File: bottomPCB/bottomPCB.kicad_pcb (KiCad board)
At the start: 2 copper layers, 184.8 x 139 mm, 47 parts, among them J1 Conn_01x03_Pin, J2 Conn_02x03_Odd_Even, J3 Conn_01x02, J4 Conn_02x03_Odd_Even, U1 ESP32-WROOM-32, U2 XT30_horizontal, U3 XT30_horizontal, U8 LM1117IMPX-3_3_NOPB, U9 LM1117IMPX-3_3_NOPB

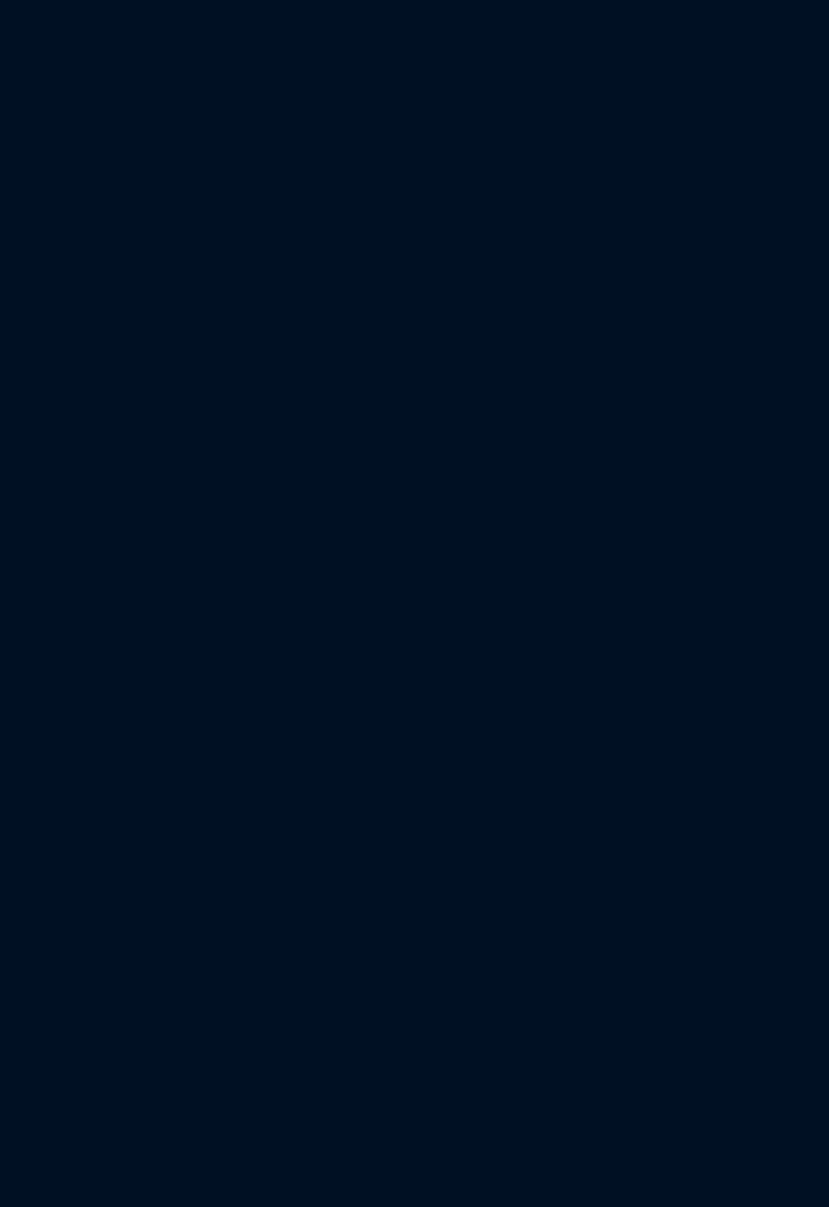
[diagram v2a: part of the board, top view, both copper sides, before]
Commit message: added vertical escon driver
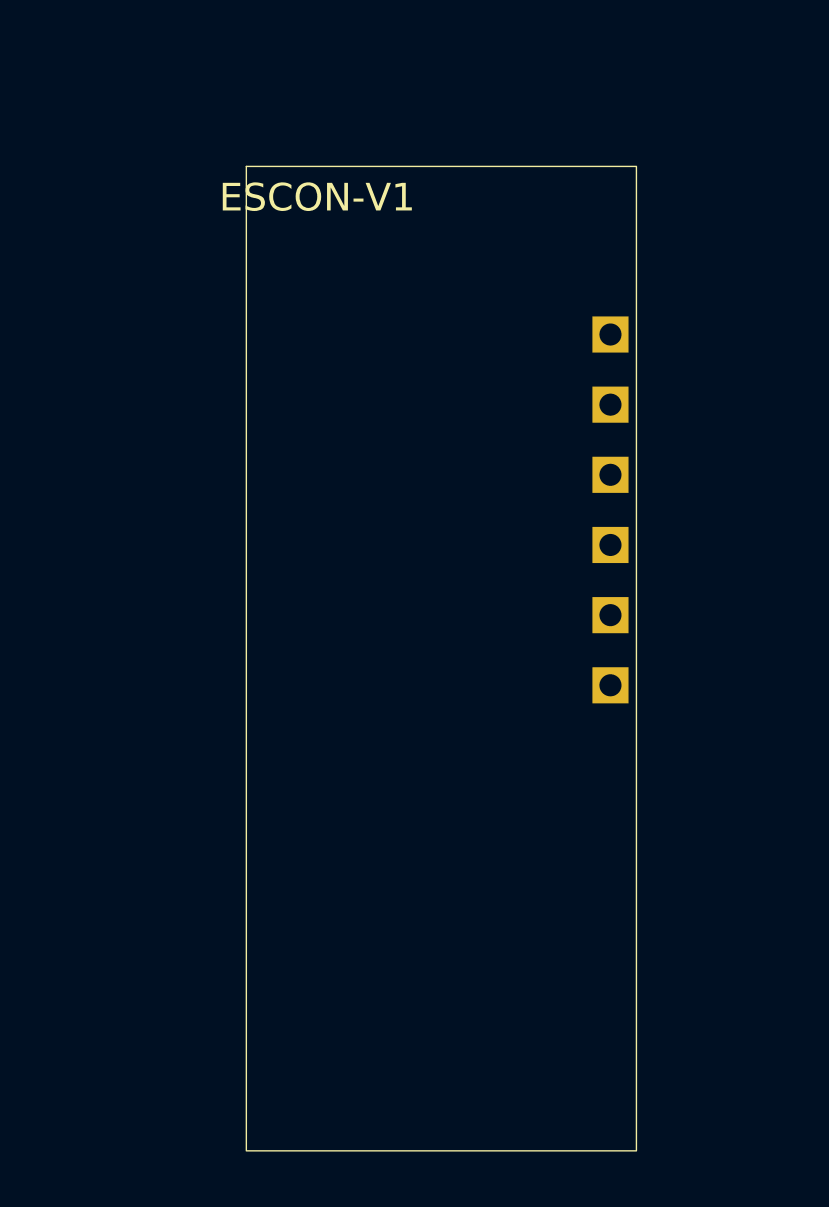
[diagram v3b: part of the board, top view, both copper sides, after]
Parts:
- added ESCON-V1: ~, sarcat:ESCON-V, F.Cu at (118.4, 98.0)
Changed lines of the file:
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@@
 	(net 86 "unconnected-(U3-Pad3)")
 	(net 87 "unconnected-(U3-Pad4)")
+	(net 88 "unconnected-(ESCON-V1-GND-Pad5)")
+	(net 89 "unconnected-(ESCON-V1-VCC-Pad6)")
+	(net 90 "unconnected-(ESCON-V1-D1-Pad1)")
+	(net 91 "unconnected-(ESCON-V1-D3-Pad3)")
+	(net 92 "unconnected-(ESCON-V1-D4-Pad4)")
+	(net 93 "unconnected-(ESCON-V1-D2-Pad2)")
 	(footprint "BohleBots:SOT-223_L6.5-W3.5-P2.30-LS7.0-BR"
 		(layer "F.Cu")
@@
 		(fp_arc
 			(start 1.390018 0.400203)
-			(mid 1.299267 0.619284)
+			(mid 1.299267 0.61928)
 			(end 1.080188 0.710033)
 			(stroke
@@
 		(tags "connector JST PH side entry")
 		(property "Reference" "JP2"
-			(at 7 -2.9 270)
+			(at 7 -2.9 -90)
 			(layer "F.SilkS")
 			(effects
@@
 		)
 		(property "Value" "B8B-PH-K"
-			(at 7 4.000001 270)
+			(at 7 4.000001 -90)
 			(layer "F.Fab")
 			(effects
@@
 				(font
 					(size 1.27 1.27)
+					(thickness 0.15)
 				)
 			)
@@
 				(font
 					(size 1.27 1.27)
+					(thickness 0.15)
 				)
 			)
@@
 				(font
 					(size 1.27 1.27)
+					(thickness 0.15)
 				)
 			)
@@
 		)
 		(fp_text user "${REFERENCE}"
-			(at 7 1.5 270)
+			(at 7 1.5 -90)
 			(layer "F.Fab")
 			(effects
@@
 		)
 	)
+	(footprint "sarcat:ESCON-V"
+		(layer "F.Cu")
+		(at 118.3786 98.0348)
+		(property "Reference" "ESCON-V1"
+			(at -4.4958 -16.6878 0)
+			(unlocked yes)
+			(layer "F.SilkS")
+			(effects
+				(font
+					(size 1 1)
+					(thickness 0.1)
+				)
+			)
+		)
+		(property "Value" "~"
+			(at -2 -9 0)
+			(unlocked yes)
+			(layer "F.Fab")
+			(effects
+				(font
+					(size 1 1)
+					(thickness 0.15)
+				)
+			)
+		)
+		(property "Footprint" "sarcat:ESCON-V"
+			(at -2 -10 0)
+			(unlocked yes)
+			(layer "F.Fab")
+			(hide yes)
+			(effects
+				(font
+					(size 1 1)
+					(thickness 0.15)
+				)
+			)
+		)
+		(property "Datasheet" ""
+			(at -2 -10 0)
+			(unlocked yes)
+			(layer "F.Fab")
+			(hide yes)
+			(effects
+				(font
+					(size 1 1)
+					(thickness 0.15)
+				)
+			)
+		)
+		(property "Description" ""
+			(at -2 -10 0)
+			(unlocked yes)
+			(layer "F.Fab")
+			(hide yes)
+			(effects
+				(font
+					(size 1 1)
+					(thickness 0.15)
+				)
+			)
+		)
+		(sheetname "Root")
+		(sheetfile "bottomPCB.kicad_sch")
+		(attr through_hole)
+		(fp_rect
+			(start -7.0612 -17.82)
+			(end 7.0612 17.82)
+			(stroke
+				(width 0.05)
+				(type default)
+			)
+			(fill none)
+			(layer "F.SilkS")
+		)
+		(fp_text user "${REFERENCE}"
+			(at -2 -7.5 0)
+			(unlocked yes)
+			(layer "F.Fab")
+			(effects
+				(font
+					(size 1 1)
+					(thickness 0.15)
+				)
+			)
+		)
+		(pad "1" thru_hole rect
+			(at 6.1214 -1.5748 90)
+			(size 1.308 1.308)
+			(drill 0.8)
+			(layers "*.Cu" "*.Mask")
+			(remove_unused_layers no)
+			(net 90 "unconnected-(ESCON-V1-D1-Pad1)")
+			(pinfunction "D1")
+			(pintype "input")
+			(thermal_bridge_angle 45)
+		)
+		(pad "2" thru_hole rect
+			(at 6.1214 -4.1148 90)
+			(size 1.308 1.308)
+			(drill 0.8)
+			(layers "*.Cu" "*.Mask")
+			(remove_unused_layers no)
+			(net 93 "unconnected-(ESCON-V1-D2-Pad2)")
+			(pinfunction "D2")
+			(pintype "input")
+			(thermal_bridge_angle 45)
+		)
+		(pad "3" thru_hole rect
+			(at 6.1214 -6.6548 90)
+			(size 1.308 1.308)
+			(drill 0.8)
+			(layers "*.Cu" "*.Mask")
+			(remove_unused_layers no)
+			(net 91 "unconnected-(ESCON-V1-D3-Pad3)")
+			(pinfunction "D3")
+			(pintype "input")
+			(thermal_bridge_angle 45)
+		)
+		(pad "4" thru_hole rect
+			(at 6.1214 -9.1948 90)
+			(size 1.308 1.308)
+			(drill 0.8)
+			(layers "*.Cu" "*.Mask")
+			(remove_unused_layers no)
+			(net 92 "unconnected-(ESCON-V1-D4-Pad4)")
+			(pinfunction "D4")
+			(pintype "input")
+			(thermal_bridge_angle 45)
+		)
+		(pad "5" thru_hole rect
+			(at 6.1214 0.9652 90)
+			(size 1.308 1.308)
+			(drill 0.8)
+			(layers "*.Cu" "*.Mask")
+			(remove_unused_layers no)
+			(net 88 "unconnected-(ESCON-V1-GND-Pad5)")
+			(pinfunction "GND")
+			(pintype "power_in")
+			(thermal_bridge_angle 45)
+		)
+		(pad "6" thru_hole rect
+			(at 6.1214 -11.7348 90)
+			(size 1.308 1.308)
+			(drill 0.8)
+			(layers "*.Cu" "*.Mask")
+			(remove_unused_layers no)
+			(net 89 "unconnected-(ESCON-V1-VCC-Pad6)")
+			(pinfunction "VCC")
+			(pintype "power_in")
+			(thermal_bridge_angle 45)
+		)
+	)
 	(footprint "BohleBots:D36V28FX"
 		(layer "F.Cu")
@@
 				(font
 					(size 1.27 1.27)
+					(thickness 0.15)
 				)
 			)
@@
 				(font
 					(size 1.27 1.27)
+					(thickness 0.15)
 				)
 			)
@@
 				(font
 					(size 1.27 1.27)
+					(thickness 0.15)
 				)
 			)
@@
 		(tags "CONN-TH_XT30PW-M footprint")
 		(property "Reference" "U3"
-			(at -0.000127 -7 270)
+			(at -0.000127 -7 -90)
 			(layer "F.SilkS")
 			(hide yes)
@@
 		)
 		(property "Value" "XT30_horizontal"
-			(at -0.000127 10.149606 270)
+			(at -0.000127 10.149606 -90)
 			(layer "F.Fab")
 			(hide yes)
@@
 				(font
 					(size 1.27 1.27)
+					(thickness 0.15)
 				)
 			)
@@
 				(font
 					(size 1.27 1.27)
+					(thickness 0.15)
 				)
 			)
@@
 				(font
 					(size 1.27 1.27)
+					(thickness 0.15)
 				)
 			)
@@
 		)
 		(fp_text user "REF**"
-			(at -0.000127 12.149606 270)
+			(at -0.000127 12.149606 -90)
 			(layer "F.Fab")
 			(effects
@@
 		(fp_arc
 			(start 1.390018 0.400203)
-			(mid 1.299267 0.619284)
+			(mid 1.299267 0.61928)
 			(end 1.080188 0.710033)
 			(stroke
@@
 				(font
 					(size 1.27 1.27)
+					(thickness 0.15)
 				)
 			)
@@
 				(font
 					(size 1.27 1.27)
+					(thickness 0.15)
 				)
 			)
@@
 				(font
 					(size 1.27 1.27)
+					(thickness 0.15)
 				)
 			)
@@
 				(font
 					(size 1.27 1.27)
+					(thickness 0.15)
 				)
 			)
@@
 				(font
 					(size 1.27 1.27)
+					(thickness 0.15)
 				)
 			)
@@
 				(font
 					(size 1.27 1.27)
+					(thickness 0.15)
 				)
 			)
@@
 				(font
 					(size 1.27 1.27)
+					(thickness 0.15)
 				)
 			)
@@
 				(font
 					(size 1.27 1.27)
+					(thickness 0.15)
 				)
 			)
@@
 				(font
 					(size 1.27 1.27)
+					(thickness 0.15)
 				)
 			)

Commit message: updated pcb
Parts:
- removed ESCON1, ESCON2, ESCON3, ESCON4: 24_2, BohleBots:ESCOM_24_2
- removed JP1, JP2, JP3, JP4: B8B-PH-K, Connector_JST:JST_PH_B8B-PH-K_1x08_P2.00mm_Vertical
- added ESCON-V1: ~, sarcat:ESCON-V, F.Cu at (-163.5, 40.0)
- added ESCON-V2: ~, sarcat:ESCON-V, F.Cu at (-148.3, 40.0)
- added ESCON-V3: ~, sarcat:ESCON-V, F.Cu at (-133.2, 40.0)
- added ESCON-V4: ~, sarcat:ESCON-V, F.Cu at (-118.0, 40.0)

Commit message: rearranged for vertical motor drivers
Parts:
- removed the ESCON-V1 at (118.4, 98.0)
- removed J1: Conn_01x03_Pin, Connector_PinSocket_2.54mm:PinSocket_1x03_P2.54mm_Vertical
- removed U2: XT30_horizontal, BohleBots:CONN-TH_XT30PW-M
- added CN2: XT30UPB-F, BohleBots:CONN-TH_XT30UPB-F, F.Cu at (16.5, 59.0)
- added ESCON-V5: ~, sarcat:ESCON-V, F.Cu at (2.00, 54.5)
- moved ESCON-V1 234.7 mm to (66.0, -9.00), turned to -90 degrees
- moved ESCON-V3 201.1 mm to (67.0, 21.0), turned to 90 degrees
- moved C-Big1 199.3 mm to (-78.8, 16.0), turned to 90 degrees
- moved A1 170.9 mm to (-74.2, -11.0), turned to -90 degrees
- moved A2 167.2 mm to (94.2, -11.0), turned to 90 degrees
- moved C6 132.5 mm to (-12.7, 1.00), turned to 180 degrees
- moved U3 132.3 mm to (-41.5, 5.00), turned to -90 degrees
- moved R8 110.7 mm to (-1.25, 81.1)
- moved R9 110.3 mm to (-1.25, 83.0)
- moved LED1 110.2 mm to (-8.00, 83.0)
- moved R10 110.1 mm to (-1.25, 85.0)
- moved ESCON-V2 103.4 mm to (-46.7, 21.0), turned to -90 degrees
- moved R7 97.9 mm to (23.7, 26.0), turned to 0 degrees
- moved C4 90.4 mm to (93.0, 4.50), turned to 90 degrees
- moved ESCON-V4 87.4 mm to (-46.0, -9.62), turned to -90 degrees
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
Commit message: added rules + changed layout
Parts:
- added I2C2: Pfostenstecker_6_2x3, BohleBots:HDR-TH_6P-P2.54-V-F-R2-C3-S2.54-4, F.Cu at (27.2, 65.0)
- moved ESCON-V2 113.7 mm to (67.0, 21.0), turned to 90 degrees
- moved ESCON-V3 113.0 mm to (-46.0, 21.0), turned to -90 degrees
- moved CN2 69.0 mm to (-27.0, 5.50)
- moved ESCON-V5 9.39 mm to (-7.38, 54.0)
- moved I2C1 8.26 mm to (27.2, 46.5), turned to -90 degrees
- moved LED1 5.51 mm to (-7.71, 77.5)
- moved R10 5.51 mm to (-0.95, 79.5)
- moved R9 5.51 mm to (-0.95, 77.5)
- moved R8 5.51 mm to (-0.95, 75.6)
- moved J4 3.04 mm to (82.0, 4.50)
- moved Prog.1 1.13 mm to (-5.31, 95.8), turned to 180 degrees
- moved Taster_LED1 1.00 mm to (19.5, 90.5)
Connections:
- U1 pad 11: PWM2 -> DIR3
- U1 pad 27: DIR2 -> PWM2
- U1 pad 28: DIR1 -> DIR2
- U1 pad 30: PWM1 -> DIR1
- U1 pad 31: DIR4 -> PWM1
- U1 pad 8: PWM4 -> DIR4
- U1 pad 9: DIR3 -> PWM4
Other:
- outline, holes or cut-outs redrawn

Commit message: set traces
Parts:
- added H1: MountingHole, BohleBots:MountingHole_4.3mm_M4, F.Cu at (11.0, -20.0)
- added H2: MountingHole, BohleBots:MountingHole_4.3mm_M4, F.Cu at (-75.0, 25.0)
- added H3: MountingHole, BohleBots:MountingHole_4.3mm_M4, F.Cu at (95.0, 25.0)
- added H4: MountingHole, BohleBots:MountingHole_4.3mm_M4, F.Cu at (10.0, 80.0)
- moved C4 99.6 mm to (11.0, 61.0), turned to -90 degrees
- moved LB-L1 26.7 mm to (86.0, -7.25), turned to 0 degrees
- moved R5 18.9 mm to (86.0, -1.25), turned to -90 degrees
- moved U8 16.5 mm to (97.0, 8.00)
- moved U9 16.5 mm to (97.0, 0.05)
- moved R11 6.27 mm to (-21.5, 18.5)
- moved R13 3.43 mm to (-21.5, 20.5)
- moved Kicker1 3.25 mm to (0.00, -25.0)
- moved R12 3.11 mm to (-21.5, 16.5)
- moved R1 2.99 mm to (7.02, -13.7)
- moved D36V28FX1 1.76 mm to (40.5, -9.46)
- moved J3 0.97 mm to (-4.00, 25.0)
- moved R4 0.58 mm to (-23.5, 25.0)
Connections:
- ESCON-V5 pad 2: unconnected-(ESCON-V5-D2-Pad2) -> +3.3V
- ESCON-V5 pad 3: unconnected-(ESCON-V5-D3-Pad3) -> +3.3V
- R13 pad 1: IN_36 -> IN_39
- R7 pad 1: Boot -> BOOT
- U1 pad 27: PWM2 -> DIR2
- U1 pad 28: DIR2 -> PWM2
- U1 pad 8: DIR4 -> PWM4
- U1 pad 9: PWM4 -> DIR4
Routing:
- net +3.3V: track 0.00 -> 483.3 mm, vias 0 -> 10
- net +BATT: track 0.00 -> 371.7 mm
- net +5V: track 0.00 -> 213.8 mm, vias 0 -> 5
- net ENA: track 0.00 -> 198.4 mm, vias 0 -> 7
- net Net-(A1-Pad3): track 0.00 -> 183.6 mm
- net SCL: track 0.00 -> 147.4 mm, vias 0 -> 6
- net EN: track 0.00 -> 123.2 mm, vias 0 -> 3
- net SDA: track 0.00 -> 121.3 mm, vias 0 -> 3
- net GND: track 0.00 -> 109.5 mm, vias 0 -> 3
- net TX: track 0.00 -> 106.4 mm, vias 0 -> 1
- net RX: track 0.00 -> 96.9 mm, vias 0 -> 1
- net BOOT: track 0.00 -> 88.1 mm, vias 0 -> 1
- net P23: track 0.00 -> 70.9 mm, vias 0 -> 4
- net LED_R: track 0.00 -> 68.9 mm, vias 0 -> 2
- net LED_G: track 0.00 -> 64.3 mm, vias 0 -> 2
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- added copper zone on B.Cu, net GND
- added copper zone on F.Cu, net GND
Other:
- board size 184.8 x 139 mm -> 184.8 x 132.4 mm

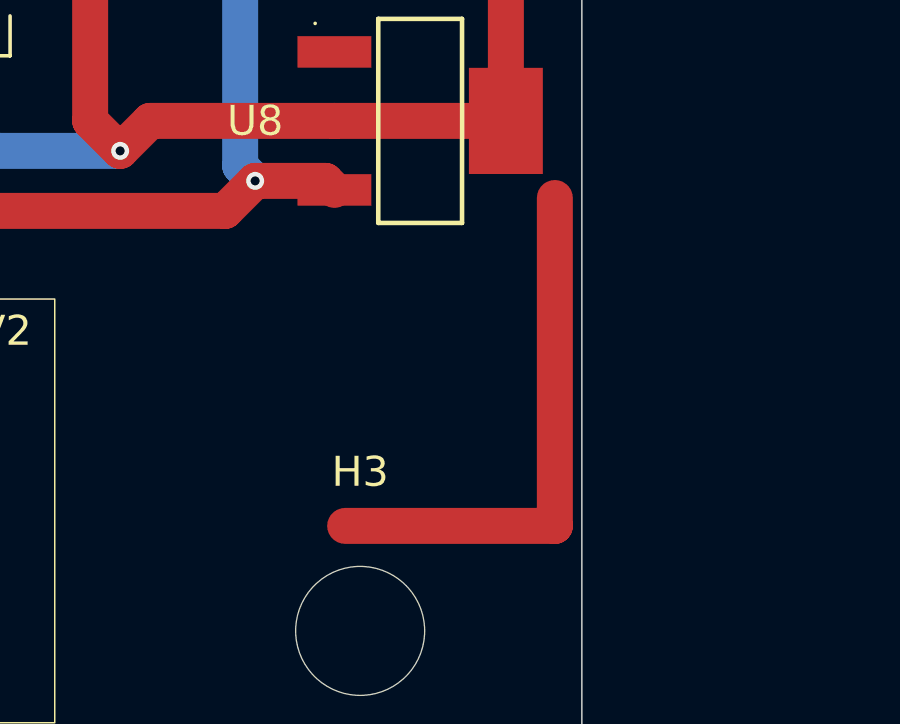
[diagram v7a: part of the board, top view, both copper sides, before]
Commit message: removed unconnected trace
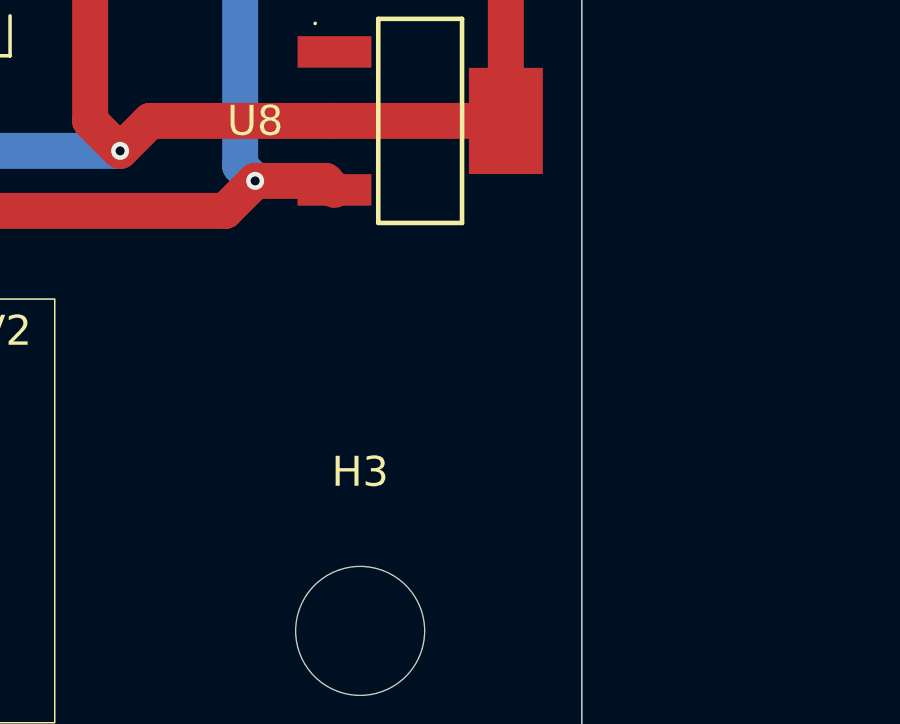
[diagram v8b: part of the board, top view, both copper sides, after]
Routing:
- net (no net): track 17.9 -> 0.00 mm
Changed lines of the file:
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@@
-	)
-	(segment
-		(start 101.49 21.5)
-		(end 101.49 10.570002)
-		(width 1.2)
-		(layer "F.Cu")
-		(net 0)
-	)
-	(segment
-		(start 94.5 21.5)
-		(end 101.49 21.5)
-		(width 1.2)
-		(layer "F.Cu")
-		(net 0)
 	)
 	(segment
